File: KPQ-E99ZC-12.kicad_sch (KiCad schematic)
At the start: 24 parts, among them J1 USB Cable, J2 Chassis, J3 SWD, J4 Edge Connector, J5 Alternate Connector, SW1 BOOT, U1 USBLC6-2SC6, U2 XC6206P332MR-G, U3 STM32C071KBT6

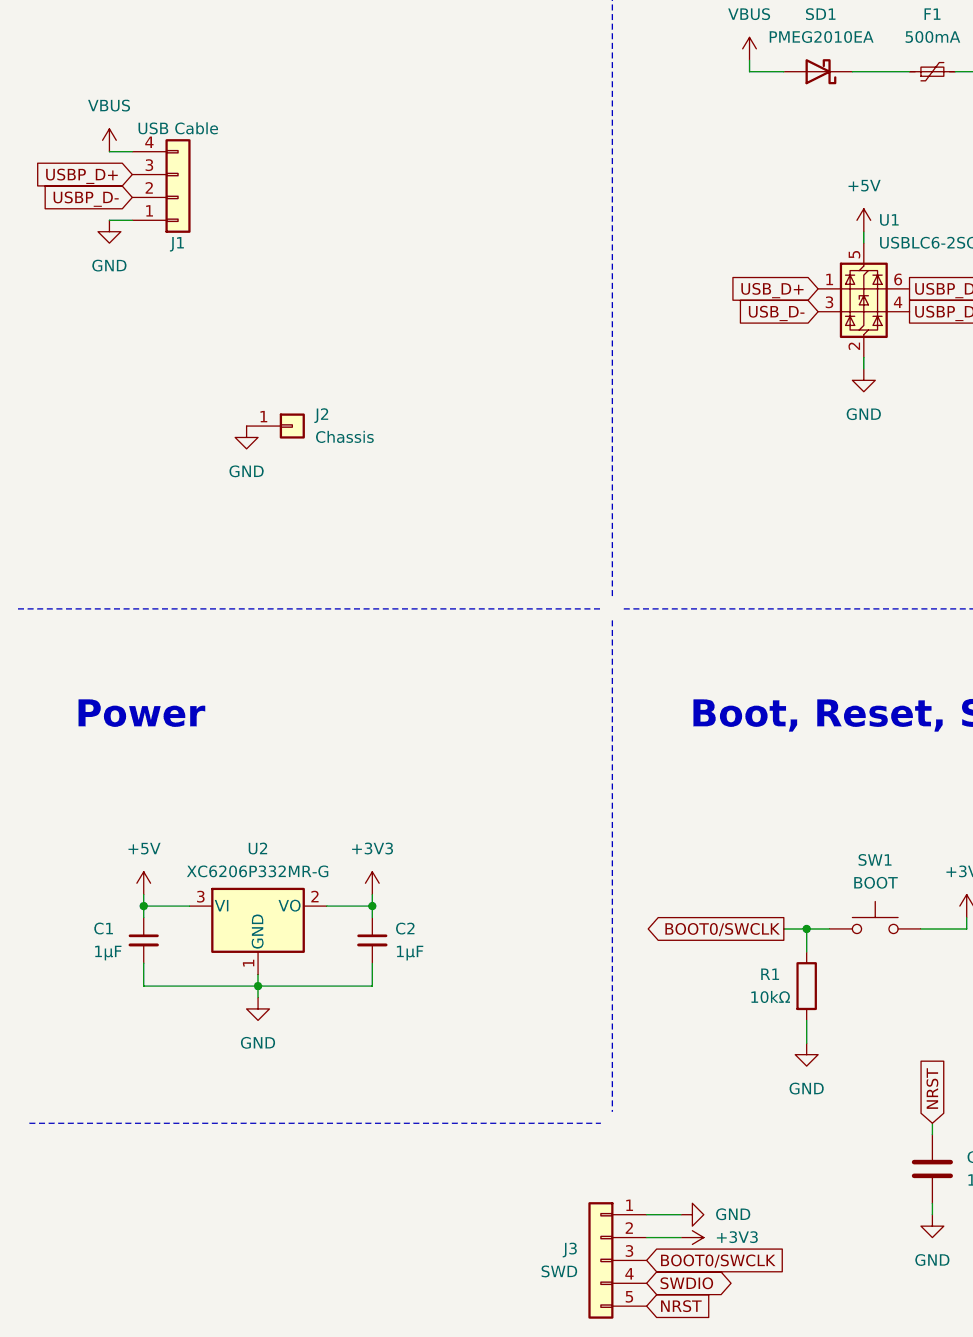
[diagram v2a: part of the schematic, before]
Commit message: Add +5V to SWD port, label SWD port, adjust PCB outline
PCB outline and LED placement adjusted after comparing printout with actual PCB.
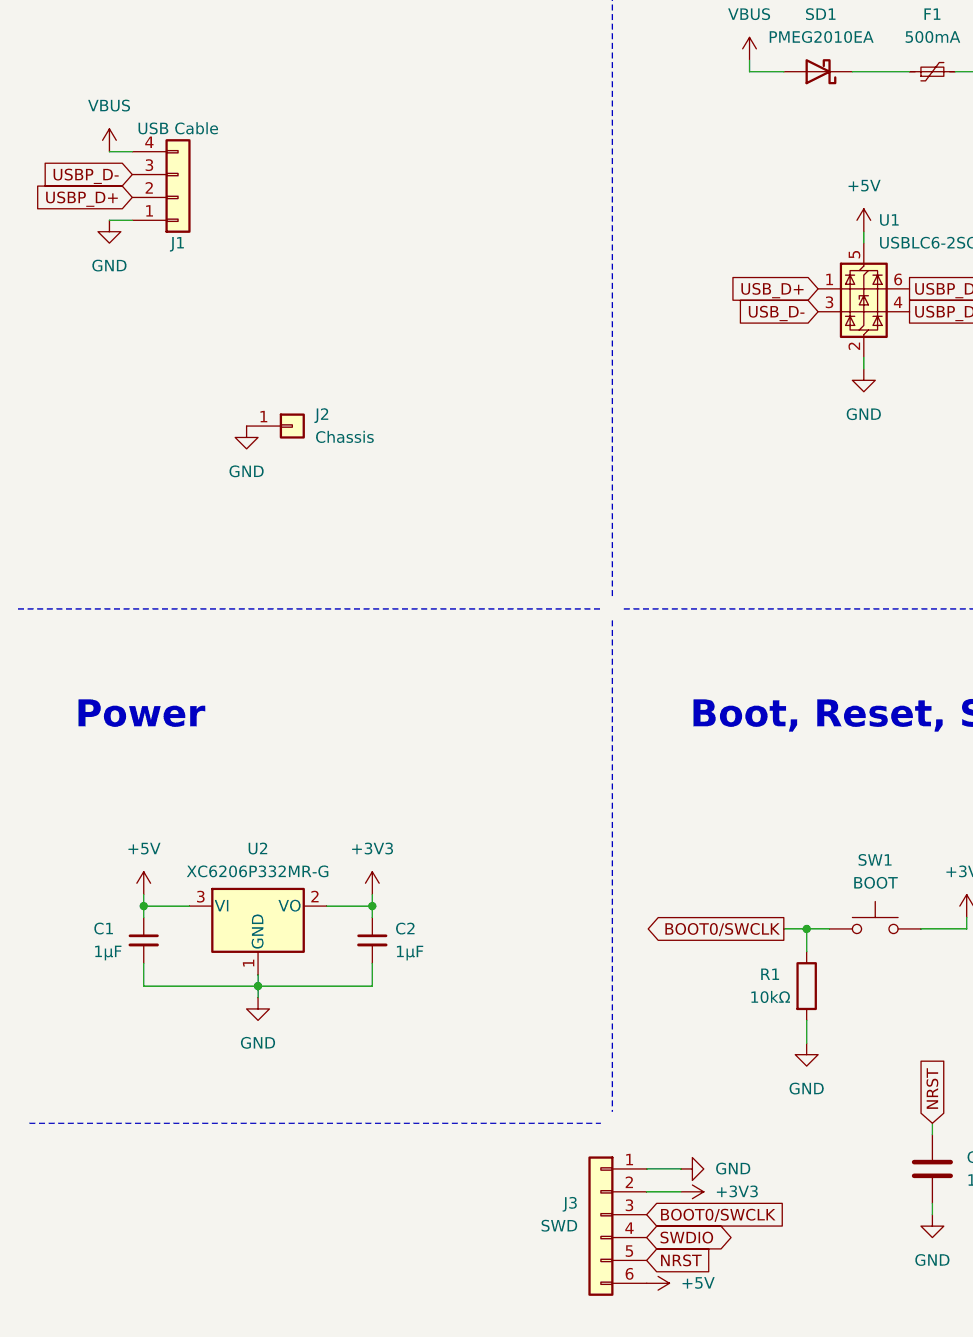
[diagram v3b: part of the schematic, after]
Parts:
- J1: footprint Connector_JST:JST_XH_S4B-XH-A_1x04_P2.50mm_Horizontal -> Connector_PinHeader_2.54mm:PinHeader_1x04_P2.54mm_Vertical
- J3: footprint Connector_PinHeader_2.00mm:PinHeader_1x05_P2.00mm_Vertical -> Project_Library:PinHeader_1x06_P2.54mm_Vertical; symbol Connector_Generic:Conn_01x05 -> Connector_Generic:Conn_01x06; P1 (none) -> GND; P2 (none) -> 3V3; P3 (none) -> CLK; P4 (none) -> I/O; P5 (none) -> RST; P6 (none) -> +5V
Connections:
- net +5V: now also J3.6 (Pin_6)
- net USBP_D+: now also J1.2 (Pin_2); no longer J1.3 (Pin_3)
- net USBP_D-: now also J1.3 (Pin_3); no longer J1.2 (Pin_2)
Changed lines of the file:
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@@
 	(wire
 		(pts
-			(xy 87.63 185.42) (xy 83.82 185.42)
+			(xy 87.63 180.34) (xy 83.82 180.34)
 		)
 		(stroke
@@
 	(wire
 		(pts
-			(xy 87.63 187.96) (xy 83.82 187.96)
+			(xy 87.63 182.88) (xy 83.82 182.88)
 		)
 		(stroke
@@
 	(global_label "NRST"
 		(shape input)
-		(at 83.82 195.58 0)
+		(at 83.82 190.5 0)
 		(fields_autoplaced yes)
 		(effects
@@
 		)
 		(property "Intersheetrefs" "${INTERSHEET_REFS}"
-			(at 90.7827 195.58 0)
+			(at 90.7827 190.5 0)
 			(effects
 				(font
@@
 	(global_label "BOOT0{slash}SWCLK"
 		(shape input)
-		(at 83.82 190.5 0)
+		(at 83.82 185.42 0)
 		(fields_autoplaced yes)
 		(effects
@@
 		)
 		(property "Intersheetrefs" "${INTERSHEET_REFS}"
-			(at 98.3153 190.5 0)
+			(at 98.3153 185.42 0)
 			(effects
 				(font
@@
 	(global_label "USBP_D+"
 		(shape input)
-		(at 26.67 69.85 180)
+		(at 26.67 72.39 180)
 		(fields_autoplaced yes)
 		(effects
@@
 		)
 		(property "Intersheetrefs" "${INTERSHEET_REFS}"
-			(at 16.7555 69.85 0)
+			(at 16.7555 72.39 0)
 			(effects
 				(font
@@
 	(global_label "SWDIO"
 		(shape bidirectional)
-		(at 83.82 193.04 0)
+		(at 83.82 187.96 0)
 		(fields_autoplaced yes)
 		(effects
@@
 		)
 		(property "Intersheetrefs" "${INTERSHEET_REFS}"
-			(at 93.0429 193.04 0)
+			(at 93.0429 187.96 0)
 			(effects
 				(font
@@
 	(global_label "USBP_D-"
 		(shape input)
-		(at 26.67 72.39 180)
+		(at 26.67 69.85 180)
 		(fields_autoplaced yes)
 		(effects
@@
 		)
 		(property "Intersheetrefs" "${INTERSHEET_REFS}"
-			(at 16.9528 72.39 0)
+			(at 16.9528 69.85 0)
 			(effects
 				(font
@@
 	)
 	(symbol
+		(lib_id "power:+5V")
+		(at 83.82 193.04 270)
+		(unit 1)
+		(exclude_from_sim no)
+		(in_bom yes)
+		(on_board yes)
+		(dnp no)
+		(fields_autoplaced yes)
+		(property "Reference" "#PWR032"
+			(at 80.01 193.04 0)
+			(effects
+				(font
+					(size 1.27 1.27)
+				)
+				(hide yes)
+			)
+		)
+		(property "Value" "+5V"
+			(at 87.63 193.04 90)
+			(effects
+				(font
+					(size 1.27 1.27)
+				)
+				(justify left)
+			)
+		)
+		(property "Footprint" ""
+			(at 83.82 193.04 0)
+			(effects
+				(font
+					(size 1.27 1.27)
+				)
+				(hide yes)
+			)
+		)
+		(property "Datasheet" ""
+			(at 83.82 193.04 0)
+			(effects
+				(font
+					(size 1.27 1.27)
+				)
+				(hide yes)
+			)
+		)
+		(property "Description" "Power symbol creates a global label with name \"+5V\""
+			(at 83.82 193.04 0)
+			(effects
+				(font
+					(size 1.27 1.27)
+				)
+				(hide yes)
+			)
+		)
+		(pin "1"
+		)
+		(instances
+			(project "KPQ-E99ZC-12"
+				(path "/2ca696f5-3b9d-4437-b6f7-98ba53a6592e"
+					(reference "#PWR032")
+					(unit 1)
+				)
+			)
+		)
+	)
+	(symbol
 		(lib_id "Regulator_Linear:XC6206PxxxMR")
 		(at 40.64 151.13 0)
@@
 	(symbol
 		(lib_id "power:GND")
-		(at 87.63 185.42 90)
+		(at 87.63 180.34 90)
 		(unit 1)
 		(exclude_from_sim no)
@@
 		(fields_autoplaced yes)
 		(property "Reference" "#PWR07"
-			(at 93.98 185.42 0)
+			(at 93.98 180.34 0)
 			(effects
 				(font
@@
 		)
 		(property "Value" "GND"
-			(at 91.44 185.42 90)
+			(at 91.44 180.34 90)
 			(effects
 				(font
@@
 		)
 		(property "Footprint" ""
-			(at 87.63 185.42 0)
+			(at 87.63 180.34 0)
 			(effects
 				(font
@@
 		)
 		(property "Datasheet" ""
-			(at 87.63 185.42 0)
+			(at 87.63 180.34 0)
 			(effects
 				(font
@@
 		)
 		(property "Description" ""
-			(at 87.63 185.42 0)
+			(at 87.63 180.34 0)
 			(effects
 				(font
@@
 	(symbol
 		(lib_id "power:+3V3")
-		(at 87.63 187.96 270)
+		(at 87.63 182.88 270)
 		(unit 1)
 		(exclude_from_sim no)
@@
 		(fields_autoplaced yes)
 		(property "Reference" "#PWR08"
-			(at 83.82 187.96 0)
+			(at 83.82 182.88 0)
 			(effects
 				(font
@@
 		)
 		(property "Value" "+3V3"
-			(at 91.44 187.96 90)
+			(at 91.44 182.88 90)
 			(effects
 				(font
@@
 		)
 		(property "Footprint" ""
-			(at 87.63 187.96 0)
+			(at 87.63 182.88 0)
 			(effects
 				(font
@@
 		)
 		(property "Datasheet" ""
-			(at 87.63 187.96 0)
+			(at 87.63 182.88 0)
 			(effects
 				(font
@@
 		)
 		(property "Description" "Power symbol creates a global label with name \"+3V3\""
-			(at 87.63 187.96 0)
+			(at 87.63 182.88 0)
 			(effects
 				(font
@@
 			)
 		)
-		(property "Footprint" "Connector_JST:JST_XH_S4B-XH-A_1x04_P2.50mm_Horizontal"
+		(property "Footprint" "Connector_PinHeader_2.54mm:PinHeader_1x04_P2.54mm_Vertical"
 			(at 31.75 72.39 0)
 			(effects
@@
 	)
 	(symbol
-		(lib_id "Connector_Generic:Conn_01x05")
-		(at 78.74 190.5 0)
+		(lib_id "Connector_Generic:Conn_01x06")
+		(at 78.74 185.42 0)
 		(mirror y)
 		(unit 1)
@@
 		(dnp no)
 		(property "Reference" "J3"
-			(at 76.2 189.23 0)
+			(at 76.2 184.15 0)
 			(effects
 				(font
@@
 		)
 		(property "Value" "SWD"
-			(at 76.2 191.77 0)
+			(at 76.2 186.69 0)
 			(effects
 				(font
@@
 			)
 		)
-		(property "Footprint" "Connector_PinHeader_2.00mm:PinHeader_1x05_P2.00mm_Vertical"
-			(at 78.74 190.5 0)
+		(property "Footprint" "Project_Library:PinHeader_1x06_P2.54mm_Vertical"
+			(at 78.74 185.42 0)
 			(effects
 				(font
@@
 		)
 		(property "Datasheet" "~"
-			(at 78.74 190.5 0)
+			(at 78.74 185.42 0)
 			(effects
 				(font
@@
 			)
 		)
-		(property "Description" "Generic connector, single row, 01x05, script generated (kicad-library-utils/schlib/autogen/connector/)"
-			(at 78.74 190.5 0)
+		(property "Description" "Generic connector, single row, 01x06, script generated (kicad-library-utils/schlib/autogen/connector/)"
+			(at 78.74 185.42 0)
+			(effects
+				(font
+					(size 1.27 1.27)
+				)
+				(hide yes)
+			)
+		)
+		(property "P1" "GND"
+			(at 78.74 185.42 0)
+			(effects
+				(font
+					(size 1.27 1.27)
+				)
+				(hide yes)
+			)
+		)
+		(property "P2" "3V3"
+			(at 78.74 185.42 0)
+			(effects
+				(font
+					(size 1.27 1.27)
+				)
+				(hide yes)
+			)
+		)
+		(property "P3" "CLK"
+			(at 78.74 185.42 0)
+			(effects
+				(font
+					(size 1.27 1.27)
+				)
+				(hide yes)
+			)
+		)
+		(property "P4" "I/O"
+			(at 78.74 185.42 0)
+			(effects
+				(font
+					(size 1.27 1.27)
+				)
+				(hide yes)
+			)
+		)
+		(property "P5" "RST"
+			(at 78.74 185.42 0)
+			(effects
+				(font
+					(size 1.27 1.27)
+				)
+				(hide yes)
+			)
+		)
+		(property "P6" "+5V"
+			(at 78.74 185.42 0)
 			(effects
 				(font
@@
 		(pin "5"
 		)
+		(pin "6"
+		)
 		(instances

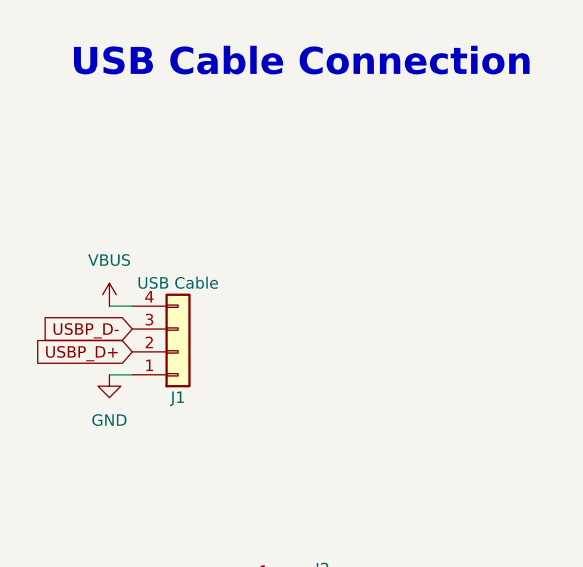
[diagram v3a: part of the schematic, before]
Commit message: Label USB post pins
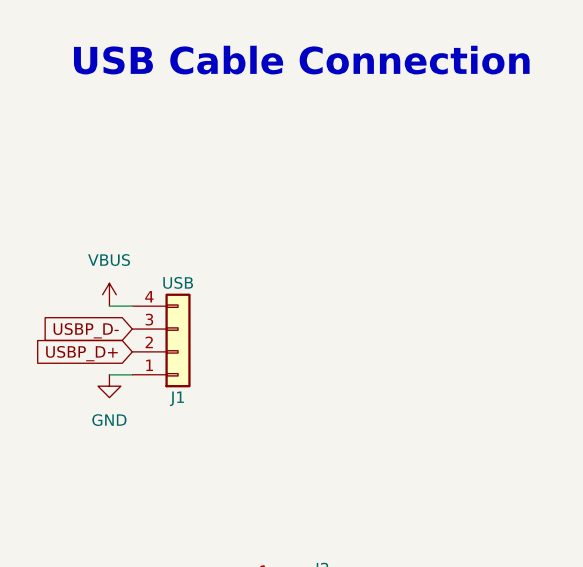
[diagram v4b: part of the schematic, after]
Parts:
- J1: value USB Cable -> USB; footprint Connector_PinHeader_2.54mm:PinHeader_1x04_P2.54mm_Vertical -> Project_Library:PinHeader_1x04_P2.54mm_Vertical; P1 (none) -> GND; P2 (none) -> D+; P3 (none) -> D-; P4 (none) -> +5V
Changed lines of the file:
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@@
 			)
 		)
-		(property "Value" "USB Cable"
+		(property "Value" "USB"
 			(at 31.75 64.77 0)
 			(effects
@@
 			)
 		)
-		(property "Footprint" "Connector_PinHeader_2.54mm:PinHeader_1x04_P2.54mm_Vertical"
+		(property "Footprint" "Project_Library:PinHeader_1x04_P2.54mm_Vertical"
 			(at 31.75 72.39 0)
 			(effects
@@
 			(at 31.75 72.39 0)
 			(effects
+				(font
+					(size 1.27 1.27)
+				)
+				(hide yes)
+			)
+		)
+		(property "P1" "GND"
+			(at 31.75 72.39 0)
+			(effects
+				(font
+					(size 1.27 1.27)
+				)
+				(hide yes)
+			)
+		)
+		(property "P2" "D+"
+			(at 31.75 72.39 0)
+			(effects
+				(font
+					(size 1.27 1.27)
+				)
+				(hide yes)
+			)
+		)
+		(property "P3" "D-"
+			(at 31.75 72.39 0)
+			(effects
+				(font
+					(size 1.27 1.27)
+				)
+				(hide yes)
+			)
+		)
+		(property "P4" "+5V"
+			(at 31.75 72.39 0)
+			(effects

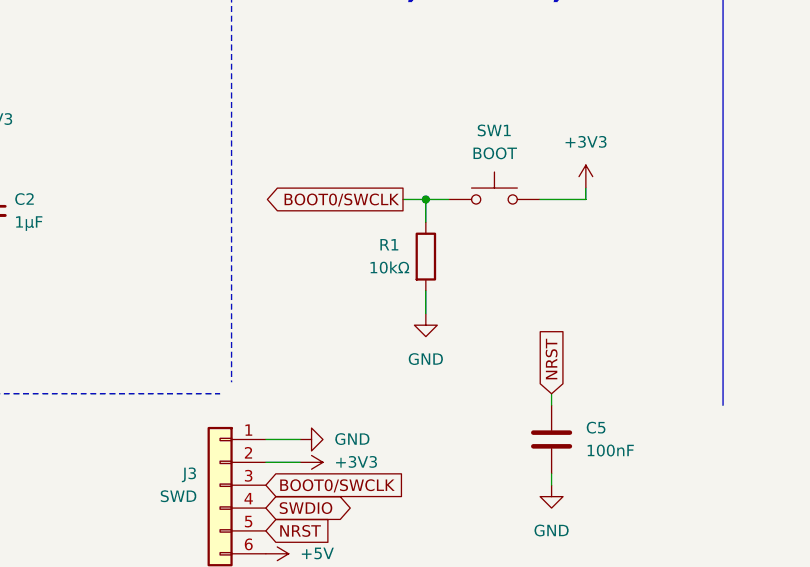
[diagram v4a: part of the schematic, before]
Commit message: Remove pull-down resistor on BOOT0
Since pin 25 is also a GPIO pin it has an internal pull-down resistor. The resistor is engaged on reset to allow for SWCLK functionality.
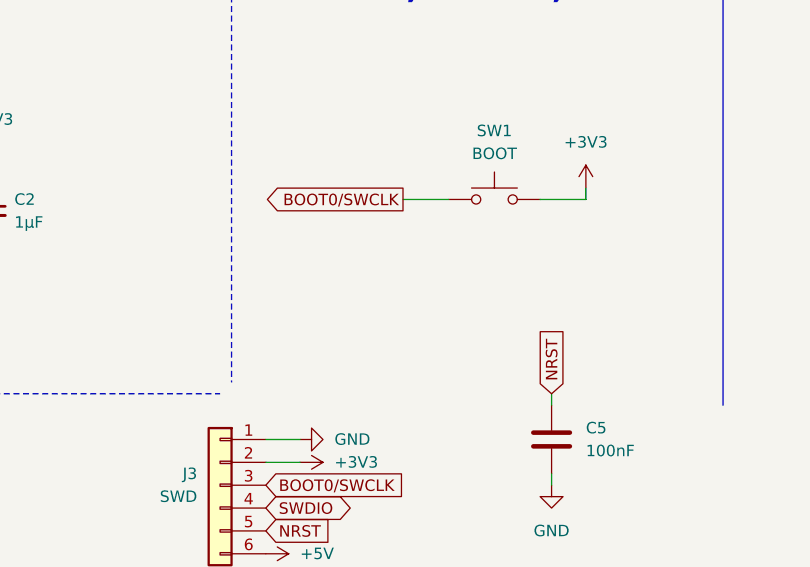
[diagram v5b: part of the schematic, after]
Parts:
- removed R1: 10kΩ, Resistor_THT:R_Axial_DIN0207_L6.3mm_D2.5mm_P7.62mm_Horizontal, symbol Device:R
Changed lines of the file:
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@@
 	)
 	(junction
-		(at 101.6 153.67)
-		(diameter 0)
-		(color 0 0 0 0)
-	)
-	(junction
 		(at 40.64 160.02)
 		(diameter 0)
@@
 	(wire
 		(pts
-			(xy 101.6 156.21) (xy 101.6 153.67)
-		)
-		(stroke
-			(width 0)
-			(type default)
-		)
-	)
-	(wire
-		(pts
 			(xy 294.64 96.52) (xy 309.88 96.52)
 		)
@@
 	(wire
 		(pts
-			(xy 99.06 153.67) (xy 101.6 153.67)
+			(xy 99.06 153.67) (xy 104.14 153.67)
 		)
 		(stroke
@@
 	(wire
 		(pts
-			(xy 101.6 163.83) (xy 101.6 166.37)
-		)
-		(stroke
-			(width 0)
-			(type default)
-		)
-	)
-	(wire
-		(pts
 			(xy 317.5 105.41) (xy 317.5 104.14)
 		)
@@
 	(wire
 		(pts
-			(xy 101.6 153.67) (xy 104.14 153.67)
-		)
-		(stroke
-			(width 0)
-			(type default)
-		)
-	)
-	(wire
-		(pts
 			(xy 40.64 161.29) (xy 40.64 160.02)
 		)
@@
 	)
 	(symbol
-		(lib_id "Device:R")
-		(at 101.6 160.02 0)
-		(unit 1)
-		(exclude_from_sim no)
-		(in_bom yes)
-		(on_board yes)
-		(dnp no)
-		(property "Reference" "R1"
-			(at 97.536 158.75 0)
-			(effects
-				(font
-					(size 1.27 1.27)
-				)
-			)
-		)
-		(property "Value" "10kΩ"
-			(at 97.536 161.29 0)
-			(effects
-				(font
-					(size 1.27 1.27)
-				)
-			)
-		)
-		(property "Footprint" "Resistor_THT:R_Axial_DIN0207_L6.3mm_D2.5mm_P7.62mm_Horizontal"
-			(at 99.822 160.02 90)
-			(effects
-				(font
-					(size 1.27 1.27)
-				)
-				(hide yes)
-			)
-		)
-		(property "Datasheet" "~"
-			(at 101.6 160.02 0)
-			(effects
-				(font
-					(size 1.27 1.27)
-				)
-				(hide yes)
-			)
-		)
-		(property "Description" "Resistor"
-			(at 101.6 160.02 0)
-			(effects
-				(font
-					(size 1.27 1.27)
-				)
-				(hide yes)
-			)
-		)
-		(pin "2"
-		)
-		(pin "1"
-		)
-		(instances
-			(project "KPQ-E99ZC-12"
-				(path "/2ca696f5-3b9d-4437-b6f7-98ba53a6592e"
-					(reference "R1")
-					(unit 1)
-				)
-			)
-		)
-	)
-	(symbol
 		(lib_id "power:GND")
 		(at 107.95 91.44 0)
@@
 					(unit 1)
 				)
-			)
-		)
-	)
-	(symbol
-		(lib_id "power:GND")
-		(at 101.6 166.37 0)
-		(unit 1)
-		(exclude_from_sim no)
-		(in_bom yes)
-		(on_board yes)
-		(dnp no)
-		(fields_autoplaced yes)
-		(property "Reference" "#PWR010"
-			(at 101.6 172.72 0)
-			(effects
-				(font
-					(size 1.27 1.27)
-				)
-				(hide yes)
-			)
-		)
-		(property "Value" "GND"
-			(at 101.6 171.45 0)
-			(effects
-				(font
-					(size 1.27 1.27)
-				)
-			)
-		)
-		(property "Footprint" ""
-			(at 101.6 166.37 0)
-			(effects
-				(font
-					(size 1.27 1.27)
-				)
-				(hide yes)
-			)
-		)
-		(property "Datasheet" ""
-			(at 101.6 166.37 0)
-			(effects
-				(font
-					(size 1.27 1.27)
-				)
-				(hide yes)
-			)
-		)
-		(property "Description" ""
-			(at 101.6 166.37 0)
-			(effects
-				(font
-					(size 1.27 1.27)
-				)
-				(hide yes)
-			)
-		)
-		(pin "1"
-		)
-		(instances
-			(project "KPQ-E99ZC-12"
-				(path "/2ca696f5-3b9d-4437-b6f7-98ba53a6592e"
-					(reference "#PWR010")
-					(unit 1)
-				)

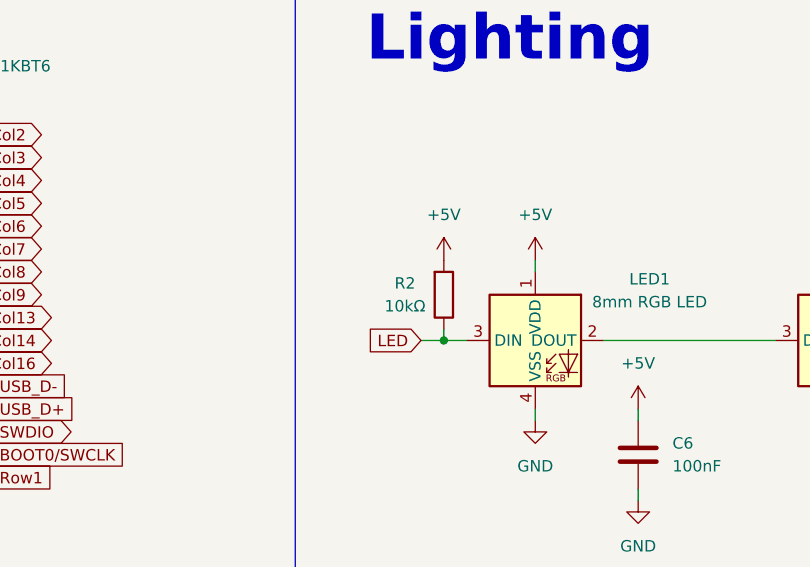
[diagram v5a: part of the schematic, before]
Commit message: Change R2 to R1 (since the previous R1 has been removed)
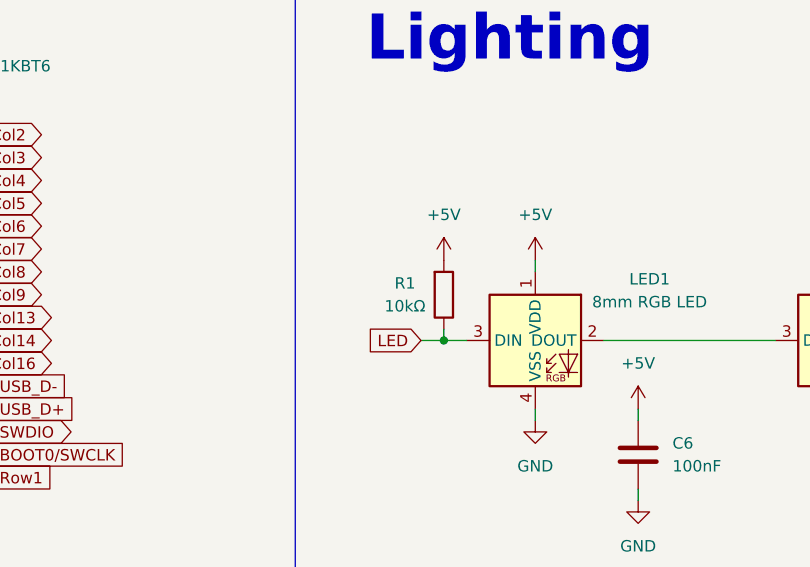
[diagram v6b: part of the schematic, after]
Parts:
- renumbered R2 to R1
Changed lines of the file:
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@@
 		(on_board yes)
 		(dnp no)
-		(property "Reference" "R2"
+		(property "Reference" "R1"
 			(at 238.252 90.17 0)
 			(effects
@@
 			(project "KPQ-E99ZC-12"
 				(path "/2ca696f5-3b9d-4437-b6f7-98ba53a6592e"
-					(reference "R2")
+					(reference "R1")
 					(unit 1)
 				)
